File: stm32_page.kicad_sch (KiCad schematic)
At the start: 42 parts, among them J1 FTSH-107-01-L-DV-K-A, J2 PZ254V-11-03P_C2937625, J4 PZ254V-11-03P_C2937625, J5 PZ254V-11-03P_C2937625, SW2 6.0*6.0*6.0, SW3 6.0*6.0*6.0, U1 STM32L431KBU6_C2826408, U4 MAX3221ECPWR, X1 SC-32S32.768kHz20PPM7pF

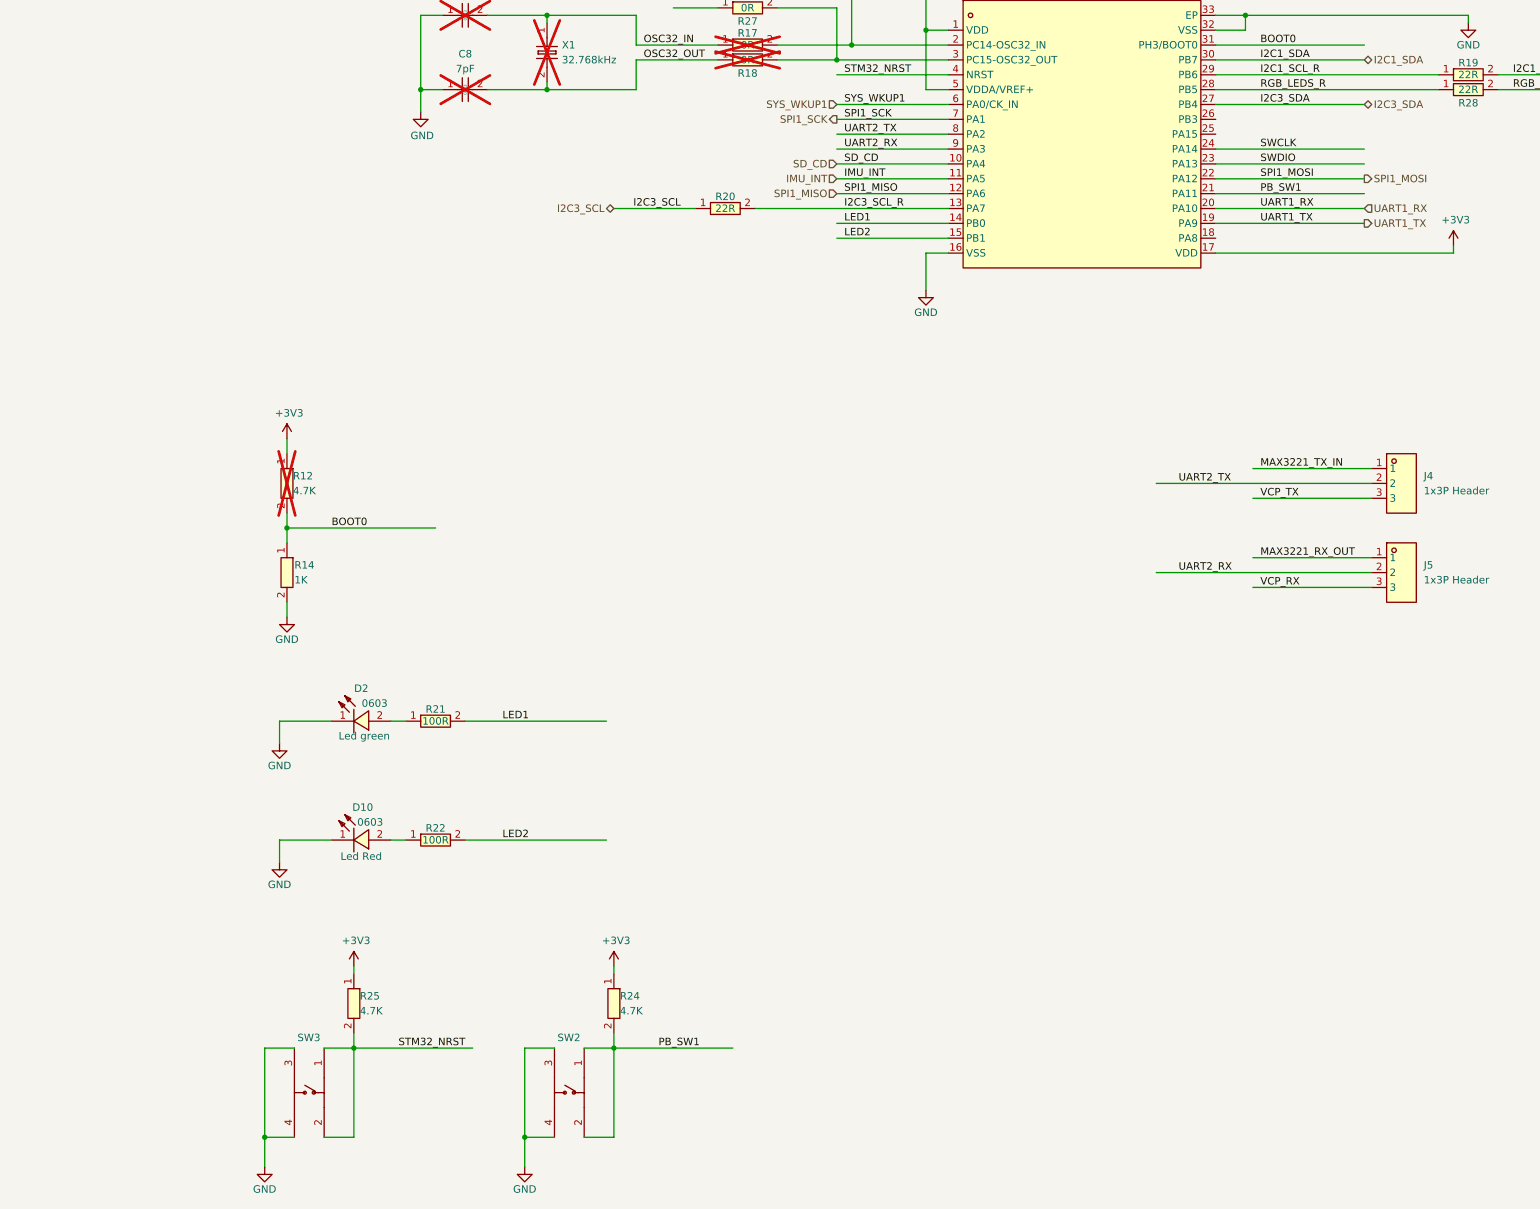
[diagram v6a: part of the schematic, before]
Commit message: Add PWM and LED. After this commit I will connect the TOP
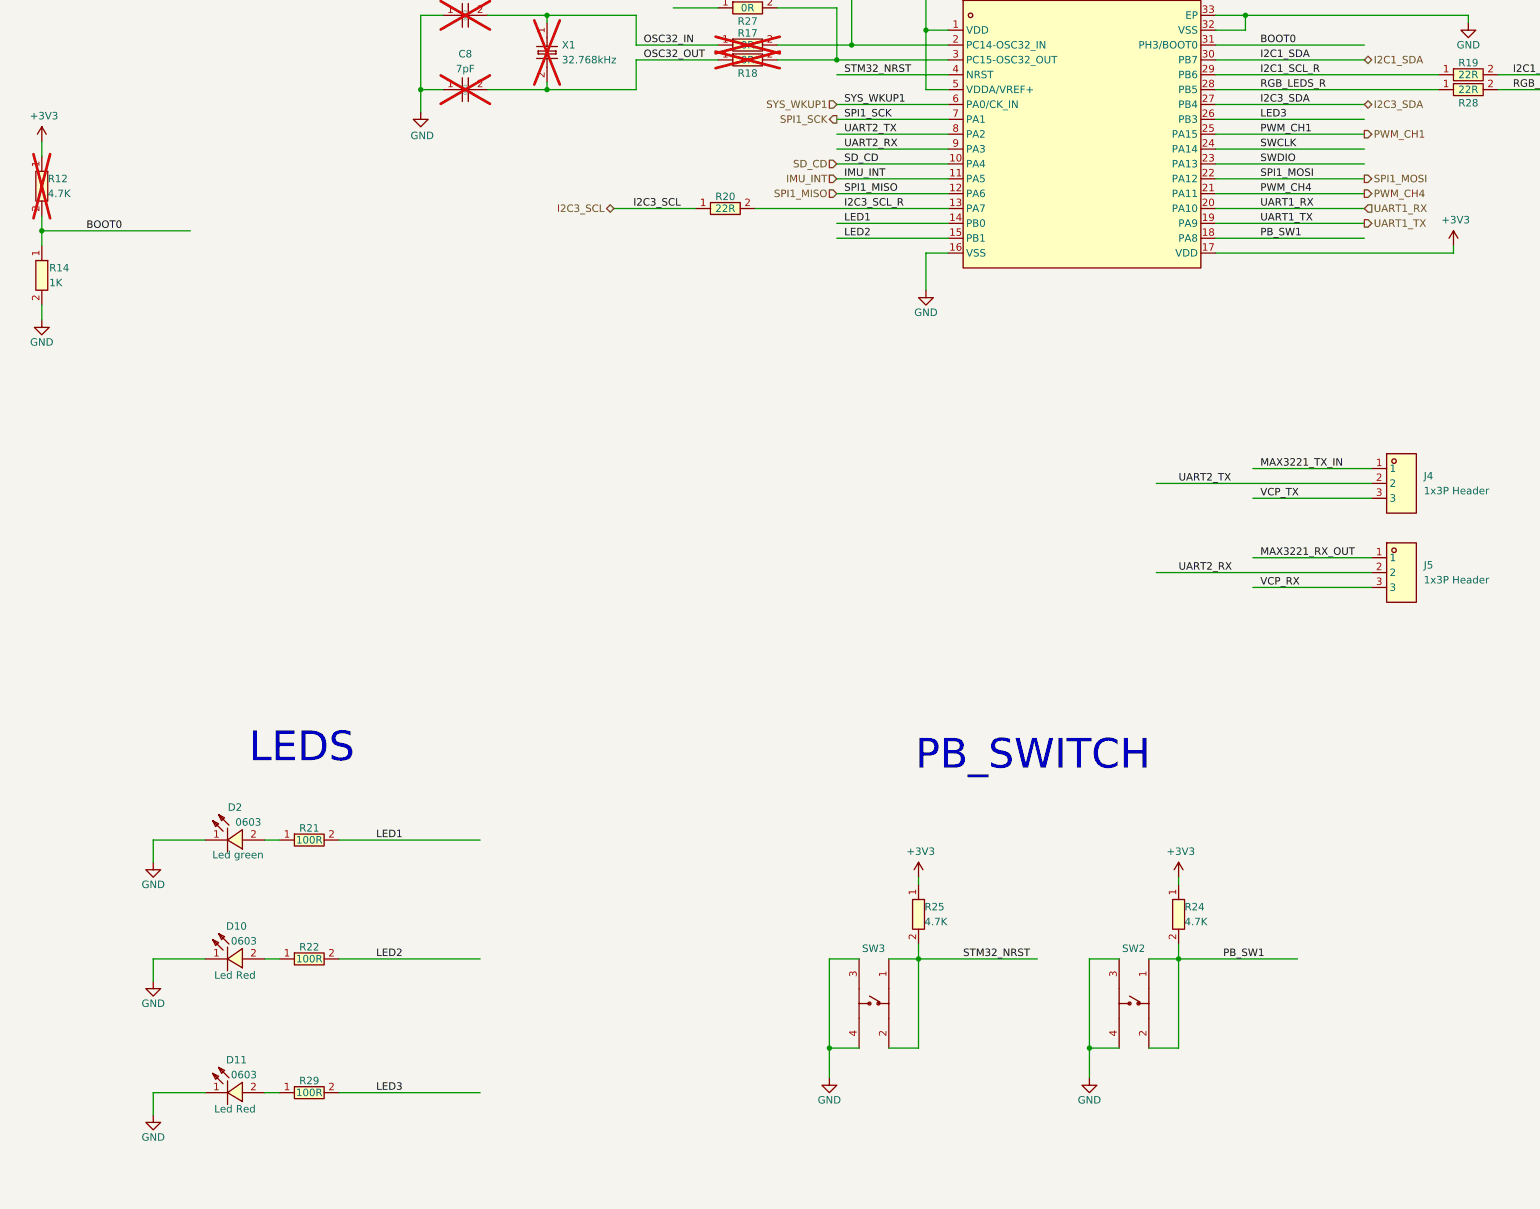
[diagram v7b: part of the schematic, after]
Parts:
- added D11: KT-0603R, easyeda2kicad:LED0603-RD, symbol easyeda2kicad:KT-0603R
- added R29: 0603WAF1000T5E, easyeda2kicad:R0603, symbol easyeda2kicad:0603WAF1000T5E
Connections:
- net GND: now also D11.1 (K)
- net PB_SW1: now also U1.18 (PA8); no longer U1.21 (PA11)
- net PWM_CH1: now reaches U1.25 (PA15)
- net LED3: now reaches U1.26 (PB3)
- net LED3: now also R29.2
- new net: D11.2 (A), R29.1
- new net PWM_CH4: U1.21 (PA11)
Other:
- note added: "LEDS"
- note added: "PB_SWITCH"
- moved on the sheet: D10, D2, R12, R14, R21, R22, R24, R25, SW2, SW3

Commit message: Finished schematic need to check , before layout
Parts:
- removed R14, R23: 0603WAF1001T5E, easyeda2kicad:R0603, symbol easyeda2kicad:0603WAF1001T5E
- removed R24, R25: 0603WAF4701T5E, easyeda2kicad:R0603, symbol easyeda2kicad:0603WAF4701T5E
- added R21, R30, R31, R36: 0603WAF1002T5E, easyeda2kicad:R0603, symbol easyeda2kicad:0603WAF1002T5E
- added TP3, TP4: TestPoint, TestPoint:TestPoint_Pad_2.0x2.0mm, symbol Connector:TestPoint
- renumbered C1 to C38, C5 to C39, C6 to C40, C11 to C41, C9 to C42, C10 to C43, C7 to C44, C8 to C45, C13 to C46, C14 to C47, C15 to C48, C12 to C49, C16 to C50, J4 to J1, J5 to J2, J1 to J4, J2 to J5, R12 to R20, R21 to R22, R22 to R23, R29 to R24, R20 to R25, R17 to R28, R18 to R29, R19 to R32, R28 to R33, R3 to R34, R2 to R40, R11 to R41, R1 to R42, SW3 to SW2, SW2 to SW3, U4 to U10
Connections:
- net +3V3: now also R30.2, R31.2
- net BOOT0: now also R21.2
- net GND: now also R21.1, R36.2
- net PB_SW1: now also R31.1
- net STM32_NRST: now also R30.1
- net at R26.1: now also TP4.1
- net at U10.1 (~{EN}): now also R36.1
- net at R27.1: now also TP3.1
